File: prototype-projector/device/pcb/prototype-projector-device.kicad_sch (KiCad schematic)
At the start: 13 parts

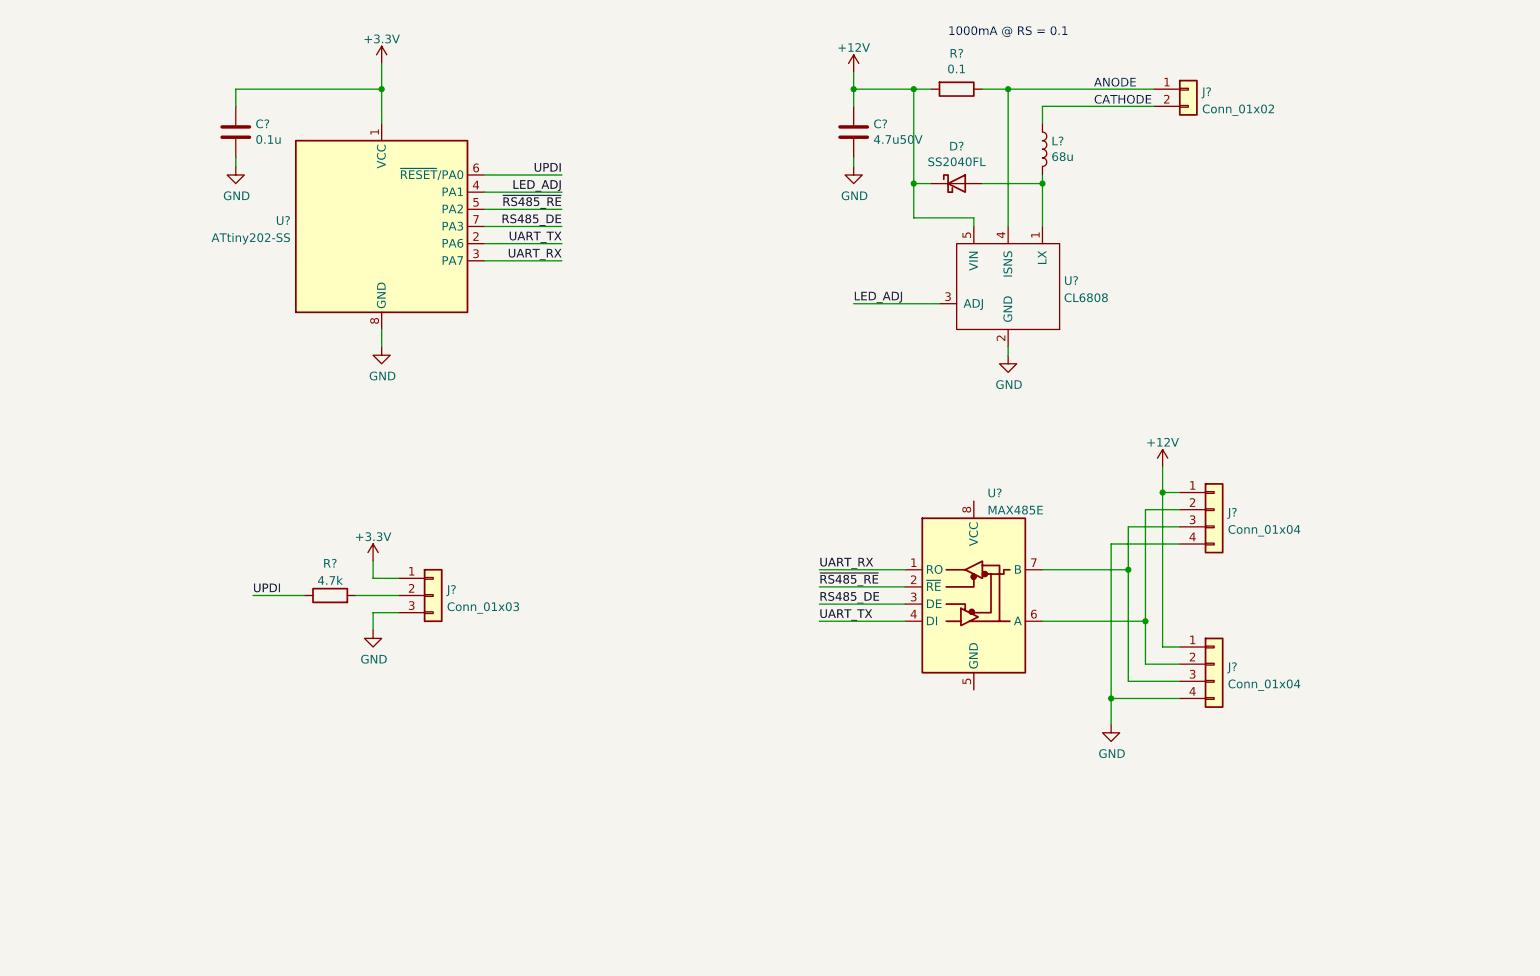
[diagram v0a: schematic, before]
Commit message: add: 回路図調整
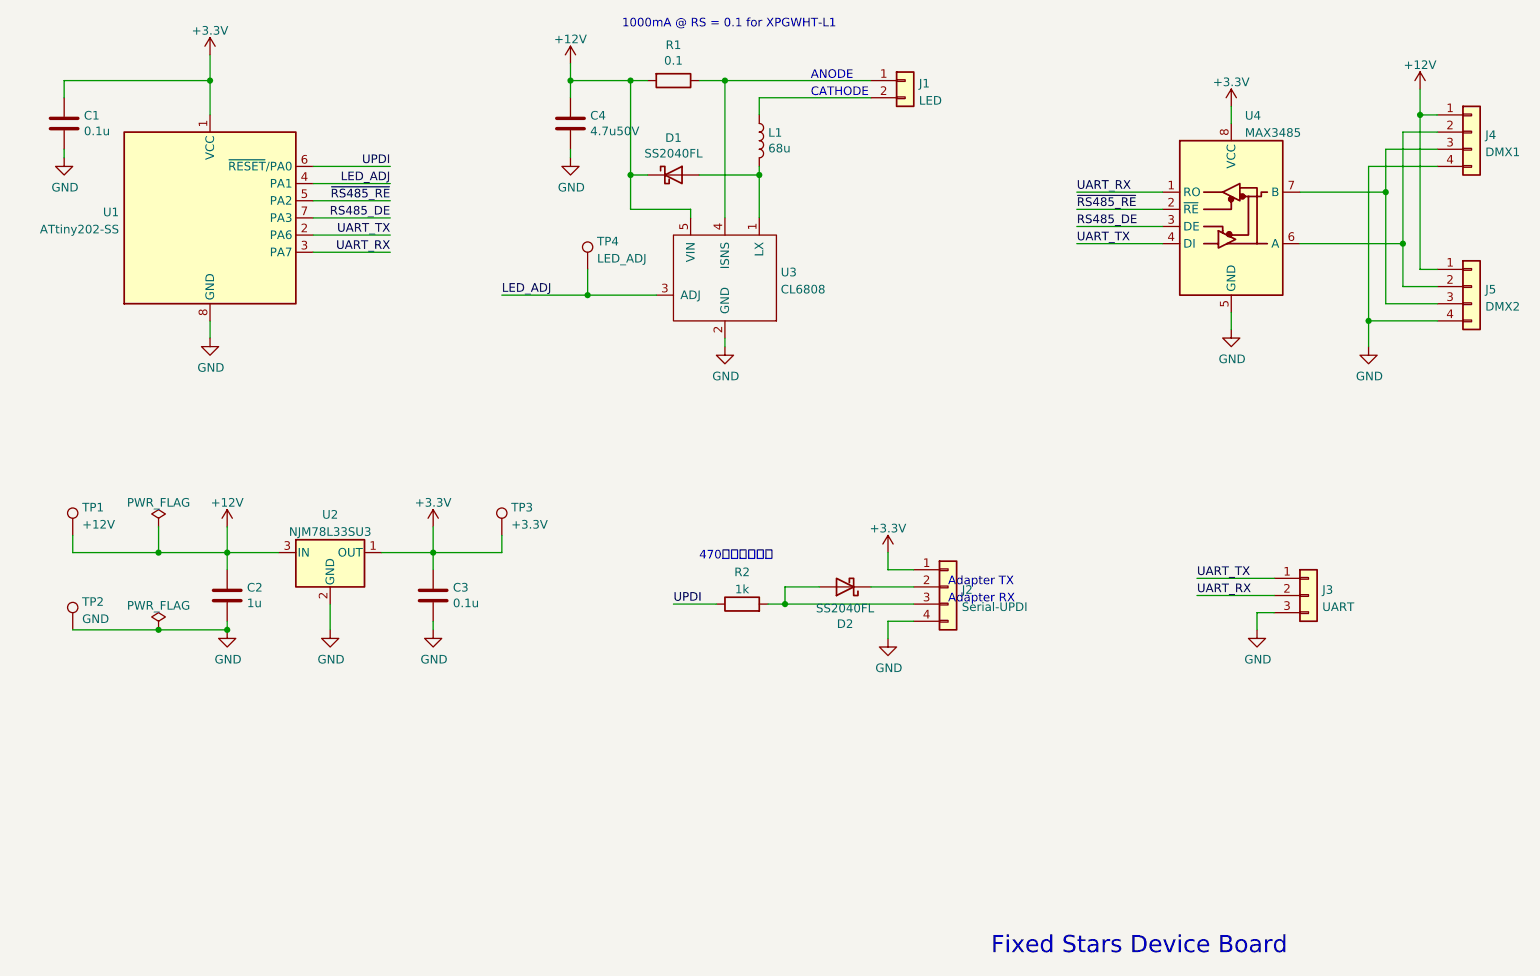
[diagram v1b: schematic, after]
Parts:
- removed J?: Conn_01x03, Connector_PinHeader_2.54mm:PinHeader_1x03_P2.54mm_Vertical, symbol Connector_Generic:Conn_01x03
- removed U?: MAX485E, Package_SO:SOP-8_3.9x4.9mm_P1.27mm, symbol Interface_UART:MAX485E
- added C2: 1u, Capacitor_SMD:C_0603_1608Metric, symbol Device:C
- added C3: 0.1u, Capacitor_SMD:C_0603_1608Metric, symbol Device:C
- added D2: SS2040FL, Diode_SMD:D_SOD-123F, symbol Device:D_Schottky
- added J2: Serial-UPDI, Connector_PinHeader_2.54mm:PinHeader_1x04_P2.54mm_Vertical, symbol Connector_Generic:Conn_01x04
- added J3: UART, Connector_PinHeader_2.54mm:PinHeader_1x03_P2.54mm_Vertical, symbol Connector_Generic:Conn_01x03
- added TP1: +12V, TestPoint:TestPoint_THTPad_D1.0mm_Drill0.5mm, symbol Connector:TestPoint
- added TP2: GND, TestPoint:TestPoint_THTPad_D1.0mm_Drill0.5mm, symbol Connector:TestPoint
- added TP3: +3.3V, TestPoint:TestPoint_THTPad_D1.0mm_Drill0.5mm, symbol Connector:TestPoint
- added TP4: LED_ADJ, TestPoint:TestPoint_THTPad_D1.0mm_Drill0.5mm, symbol Connector:TestPoint
- added U2: NJM78L33SU3, Package_TO_SOT_SMD:SOT-89-3, symbol Regulator_Linear:L78L33_SOT89
- added U4: MAX3485, Package_SO:SOP-8_3.9x4.9mm_P1.27mm, symbol Interface_UART:MAX3485
- C1: renamed from C?; footprint Capacitor_SMD:C_0805_2012Metric -> Capacitor_SMD:C_0603_1608Metric
- J1: renamed from J?; value Conn_01x02 -> LED
- J4: renamed from J?; value Conn_01x04 -> DMX1; footprint (none) -> Connector_JST:JST_XH_B4B-XH-A_1x04_P2.50mm_Vertical
- J5: renamed from J?; value Conn_01x04 -> DMX2; footprint (none) -> Connector_JST:JST_XH_B4B-XH-A_1x04_P2.50mm_Vertical
- R2: renamed from R?; value 4.7k -> 1k; footprint (none) -> Resistor_SMD:R_0603_1608Metric
- gave numbers to parts that had none: 6
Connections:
- net +12V: now also C2.1, TP1.1, U2.3 (IN)
- net +3.3V: now also C3.1, J2.1 (Pin_1), TP3.1, U2.1 (OUT), U4.8 (VCC)
- net GND: now also C2.2, C3.2, J2.4 (Pin_4), J3.3 (Pin_3), TP2.1, U2.2 (GND), U4.5 (GND)
- net LED_ADJ: now also TP4.1
- net RS485_DE: now also U4.3 (DE)
- net UART_RX: now also J3.2 (Pin_2), U4.1 (RO)
- net UART_TX: now also J3.1 (Pin_1), U4.4 (DI)
- net ~{RS485_RE}: now also U4.2 (~{RE})
- net at J4.2 (Pin_2), J5.2 (Pin_2): now also U4.6 (A)
- net at J4.3 (Pin_3), J5.3 (Pin_3): now also U4.7 (B)
- net at R2.2: now also D2.2 (A), J2.3 (Pin_3)
- new net: D2.1 (K), J2.2 (Pin_2)
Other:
- note added: "1000mA @ RS = 0.1 for XPGWHT-L1"
- note added: "470が買いにくい"
- note added: "Adapter RX"
- note added: "Adapter TX"
- note added: "Fixed Stars Device Board"
- note removed: "1000mA @ RS = 0.1"
- moved on the sheet: C1, C4, D1, J1, J4, J5, L1, R1, R2, U1, U3

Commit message: add: 配線
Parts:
- J1: footprint Connector_Wire:SolderWire-2.5sqmm_1x02_P7.2mm_D2.4mm_OD3.6mm_Relief -> Connector_Wire:SolderWire-0.25sqmm_1x02_P4.2mm_D0.65mm_OD1.7mm_Relief
- TP1, TP2, TP3: footprint TestPoint:TestPoint_THTPad_D1.0mm_Drill0.5mm -> TestPoint:TestPoint_THTPad_D2.0mm_Drill1.0mm
- TP4: value LED_ADJ -> ADJ; footprint TestPoint:TestPoint_THTPad_D1.0mm_Drill0.5mm -> TestPoint:TestPoint_THTPad_D2.0mm_Drill1.0mm
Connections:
- net RS485_DE: now also U1.5 (PA2); no longer U1.7 (PA3)
- net ~{RS485_RE}: now also U1.7 (PA3); no longer U1.5 (PA2)
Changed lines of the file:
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@@
     (effects (font (size 1.27 1.27)) (justify right bottom))
   )
-  (label "~{RS485_RE}" (at 91.44 64.77 180)
+  (label "RS485_DE" (at 91.44 64.77 180)
     (effects (font (size 1.27 1.27)) (justify right bottom))
   )
@@
     (effects (font (size 1.27 1.27)) (justify right bottom))
   )
-  (label "RS485_DE" (at 91.44 67.31 180)
+  (label "~{RS485_RE}" (at 91.44 67.31 180)
     (effects (font (size 1.27 1.27)) (justify right bottom))
   )
@@
       (effects (font (size 1.27 1.27)) (justify left))
     )
-    (property "Footprint" "TestPoint:TestPoint_THTPad_D1.0mm_Drill0.5mm" (id 2) (at 113.03 114.3 0)
+    (property "Footprint" "TestPoint:TestPoint_THTPad_D2.0mm_Drill1.0mm" (id 2) (at 113.03 114.3 0)
       (effects (font (size 1.27 1.27)) hide)
     )
@@
       (effects (font (size 1.27 1.27)) (justify left))
     )
-    (property "Footprint" "Connector_Wire:SolderWire-2.5sqmm_1x02_P7.2mm_D2.4mm_OD3.6mm_Relief" (id 2) (at 167.64 46.99 0)
+    (property "Footprint" "Connector_Wire:SolderWire-0.25sqmm_1x02_P4.2mm_D0.65mm_OD1.7mm_Relief" (id 2) (at 167.64 46.99 0)
       (effects (font (size 1.27 1.27)) hide)
     )
@@
       (effects (font (size 1.27 1.27)) (justify left))
     )
-    (property "Footprint" "TestPoint:TestPoint_THTPad_D1.0mm_Drill0.5mm" (id 2) (at 49.53 114.3 0)
+    (property "Footprint" "TestPoint:TestPoint_THTPad_D2.0mm_Drill1.0mm" (id 2) (at 49.53 114.3 0)
       (effects (font (size 1.27 1.27)) hide)
     )
@@
       (effects (font (size 1.27 1.27)) (justify left))
     )
-    (property "Footprint" "TestPoint:TestPoint_THTPad_D1.0mm_Drill0.5mm" (id 2) (at 49.53 128.27 0)
+    (property "Footprint" "TestPoint:TestPoint_THTPad_D2.0mm_Drill1.0mm" (id 2) (at 49.53 128.27 0)
       (effects (font (size 1.27 1.27)) hide)
     )
@@
       (effects (font (size 1.27 1.27)) (justify left))
     )
-    (property "Value" "LED_ADJ" (id 1) (at 122.047 73.3302 0)
-      (effects (font (size 1.27 1.27)) (justify left))
-    )
-    (property "Footprint" "TestPoint:TestPoint_THTPad_D1.0mm_Drill0.5mm" (id 2) (at 125.73 74.93 0)
+    (property "Value" "ADJ" (id 1) (at 122.047 73.3302 0)
+      (effects (font (size 1.27 1.27)) (justify left))
+    )
+    (property "Footprint" "TestPoint:TestPoint_THTPad_D2.0mm_Drill1.0mm" (id 2) (at 125.73 74.93 0)
       (effects (font (size 1.27 1.27)) hide)
     )
@@
     )
     (path "/53739052-2425-422a-baf8-cba654535b0f"
-      (reference "J1") (unit 1) (value "LED") (footprint "Connector_Wire:SolderWire-2.5sqmm_1x02_P7.2mm_D2.4mm_OD3.6mm_Relief")
+      (reference "J1") (unit 1) (value "LED") (footprint "Connector_Wire:SolderWire-0.25sqmm_1x02_P4.2mm_D0.65mm_OD1.7mm_Relief")
     )
     (path "/f064a48f-7f37-48a3-9f20-139b3263db00"
@@
     )
     (path "/9b3e521f-dacc-439a-b418-7d1ac6ead2ba"
-      (reference "TP1") (unit 1) (value "+12V") (footprint "TestPoint:TestPoint_THTPad_D1.0mm_Drill0.5mm")
+      (reference "TP1") (unit 1) (value "+12V") (footprint "TestPoint:TestPoint_THTPad_D2.0mm_Drill1.0mm")
     )
     (path "/c7036316-2fd2-4fc4-b239-a2b25e857406"
-      (reference "TP2") (unit 1) (value "GND") (footprint "TestPoint:TestPoint_THTPad_D1.0mm_Drill0.5mm")
+      (reference "TP2") (unit 1) (value "GND") (footprint "TestPoint:TestPoint_THTPad_D2.0mm_Drill1.0mm")
     )
     (path "/15c3fd5f-abf4-456d-afca-283dbe9ed62f"
-      (reference "TP3") (unit 1) (value "+3.3V") (footprint "TestPoint:TestPoint_THTPad_D1.0mm_Drill0.5mm")
+      (reference "TP3") (unit 1) (value "+3.3V") (footprint "TestPoint:TestPoint_THTPad_D2.0mm_Drill1.0mm")
     )
     (path "/f19381c4-6e2e-42c4-8725-ccf2b310d4a5"
-      (reference "TP4") (unit 1) (value "LED_ADJ") (footprint "TestPoint:TestPoint_THTPad_D1.0mm_Drill0.5mm")
+      (reference "TP4") (unit 1) (value "ADJ") (footprint "TestPoint:TestPoint_THTPad_D2.0mm_Drill1.0mm")
     )
     (path "/15238ea1-96e6-4740-9d4a-ab96db0c8626"
